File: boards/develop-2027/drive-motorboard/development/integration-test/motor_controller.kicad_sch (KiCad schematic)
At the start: 28 parts, among them U1 STSPIN32G0A2

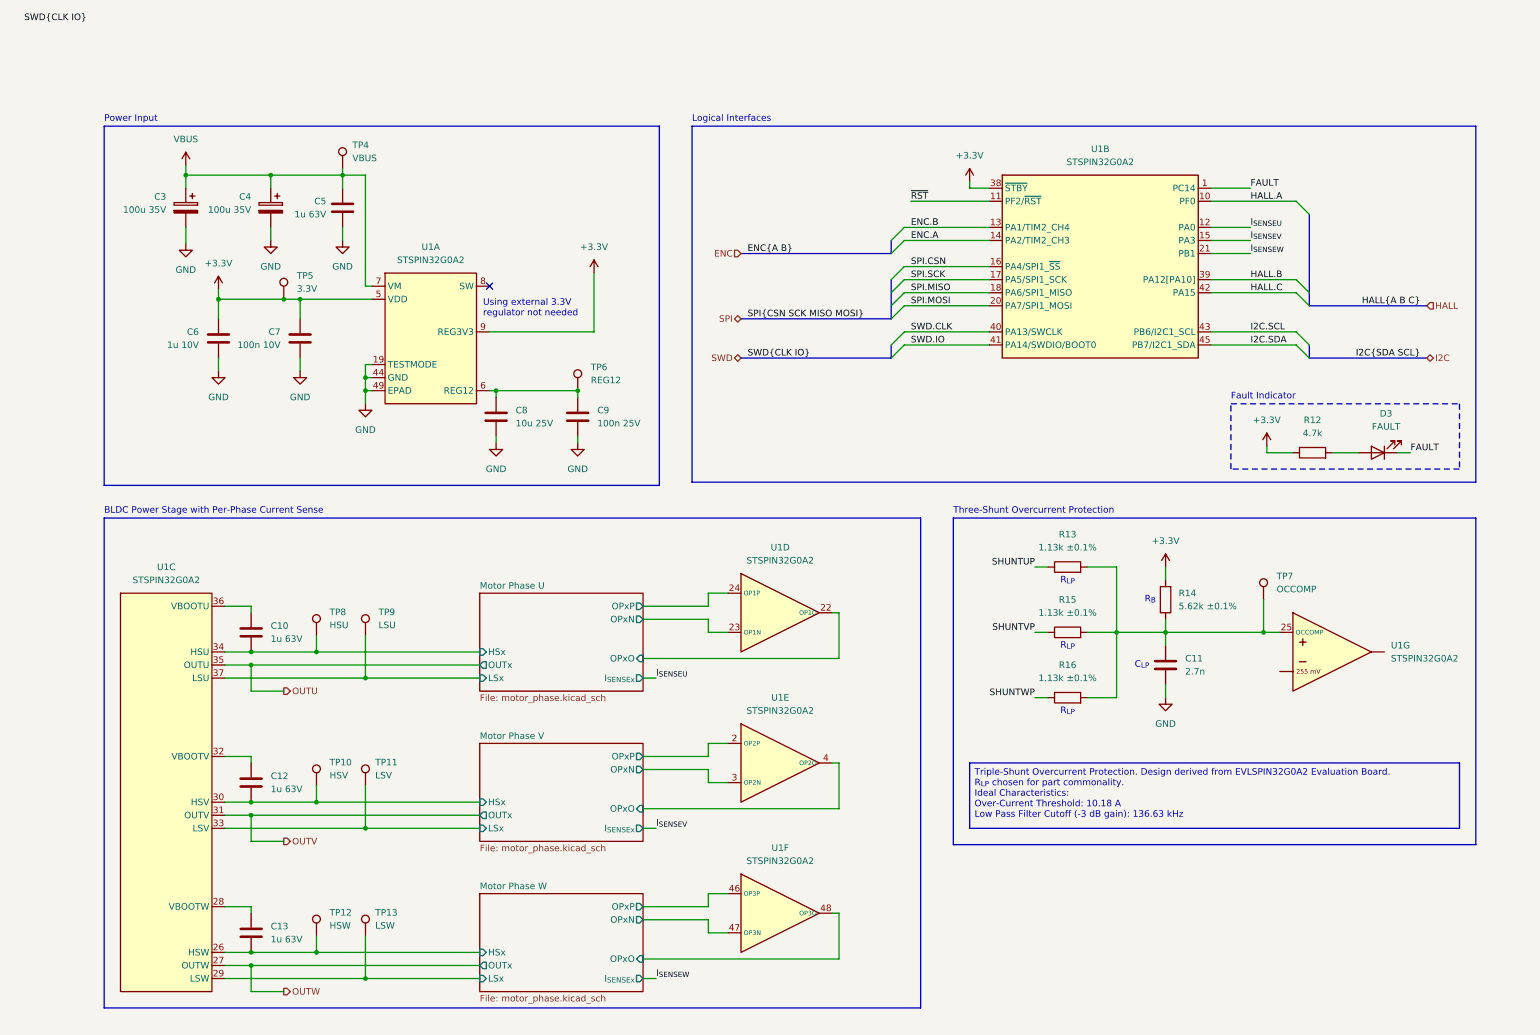
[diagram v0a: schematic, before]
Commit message: Resolve all ERC, tweak formatting
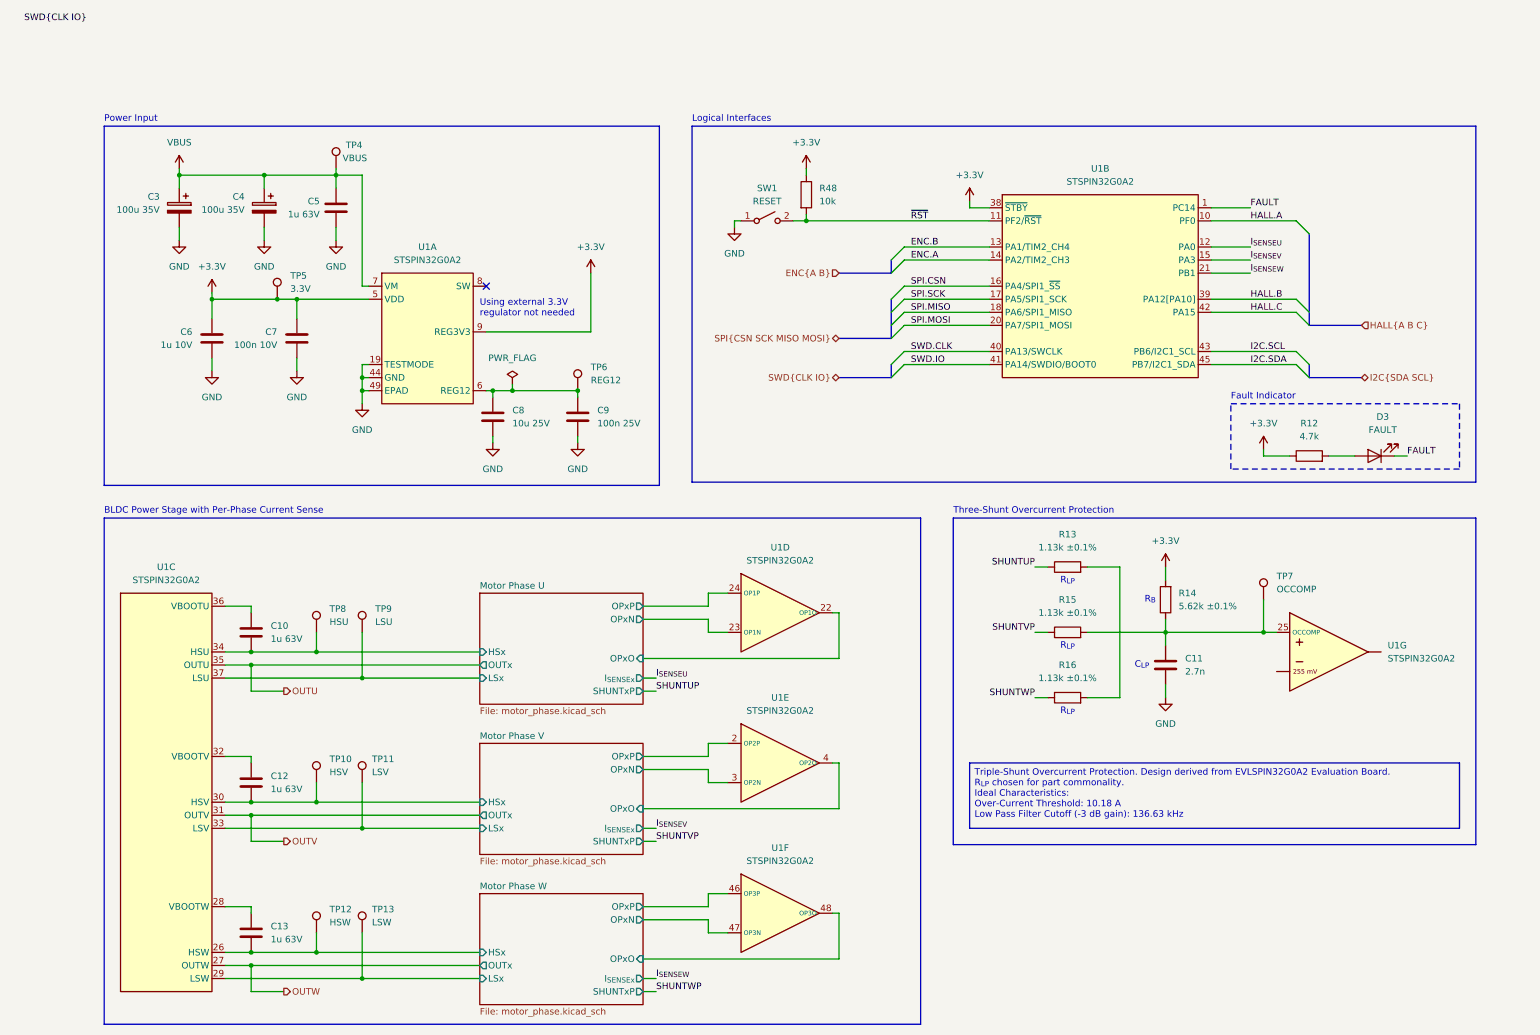
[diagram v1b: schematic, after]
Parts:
- added R48: 10k, Resistor_SMD:R_0402_1005Metric, symbol Device:R
- added SW1: RESET, Button_Switch_SMD:SW_Push_1P1T_NO_CK_KMR2, symbol Switch:SW_SPST
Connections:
- net +3.3V: now also R48.1
- net GND: now also SW1.1 (A)
- net ~{RST}: now also R48.2, SW1.2 (B)
- net at C11.1, R14.1, R15.2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: no longer R13.2, R16.2
- new net: R13.2, R16.2
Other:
- sheet Motor Phase U ports: added SHUNTxP; removed none
- sheet Motor Phase V ports: added SHUNTxP; removed none
- sheet Motor Phase W ports: added SHUNTxP; removed none
- moved on the sheet: C3, C4, C5, C6, C7, C8, D3, R12, TP10, TP11, TP12, TP13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

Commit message: tweak issues found during review, prep for single-shunt current sense
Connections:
- net ENC.A: now also U1.18 (PA6/TIM3_CH1); no longer U1.14 (PA2/TIM2_CH3)
- net ENC.B: now also U1.20 (PA7/TIM3_CH2); no longer U1.13 (PA1/TIM2_CH4)
- net HALL.A: now also U1.12 (PA0/TIM2_CH1); no longer U1.10 (PF0)
- net HALL.B: now also U1.13 (PA1/TIM2_CH2); no longer U1.39 (PA12[PA10])
- net HALL.C: now also U1.14 (PA2/TIM2_CH3); no longer U1.42 (PA15)
- net I_{SENSEU}: no longer U1.12 (PA0)
- net I_{SENSEV}: no longer U1.15 (PA3)
- net I_{SENSEW}: no longer U1.21 (PB1)
- net SPI.MISO: now also U1.15 (PA3/SPI2_MISO); no longer U1.18 (PA6/SPI1_MISO)
- net SPI.MOSI: now also U1.39 (PA12[PA10]/SPI2_MOSI); no longer U1.20 (PA7/SPI1_MOSI)
- new net I_{SENSE}: U1.21 (PB1)
- no-connect marks 1 -> 3
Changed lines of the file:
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@@
 		(at 90.17 53.34)
+	)
+	(no_connect
+		(at 231.14 40.64)
+	)
+	(no_connect
+		(at 231.14 55.88)
 	)
 	(bus_entry
@@
 	)
 	(bus_entry
-		(at 247.65 55.88)
+		(at 247.65 48.26)
 		(size 2.54 2.54)
 		(stroke
@@
 	)
 	(bus_entry
-		(at 247.65 58.42)
+		(at 247.65 50.8)
 		(size 2.54 2.54)
 		(stroke
@@
 	)
 	(bus_entry
-		(at 247.65 40.64)
+		(at 247.65 45.72)
 		(size 2.54 2.54)
 		(stroke
@@
 	(wire
 		(pts
-			(xy 231.14 55.88) (xy 247.65 55.88)
+			(xy 231.14 48.26) (xy 247.65 48.26)
 		)
 		(stroke
@@
 	(wire
 		(pts
+			(xy 231.14 60.96) (xy 238.76 60.96)
+		)
+		(stroke
+			(width 0)
+			(type default)
+		)
+	)
+	(wire
+		(pts
 			(xy 241.3 85.09) (xy 241.3 86.36)
 		)
@@
 	(wire
 		(pts
-			(xy 231.14 58.42) (xy 247.65 58.42)
+			(xy 231.14 50.8) (xy 247.65 50.8)
 		)
 		(stroke
@@
 	(wire
 		(pts
-			(xy 231.14 50.8) (xy 238.76 50.8)
-		)
-		(stroke
-			(width 0)
-			(type default)
-		)
-	)
-	(wire
-		(pts
 			(xy 50.8 161.29) (xy 44.45 161.29)
 		)
@@
 	(wire
 		(pts
-			(xy 231.14 48.26) (xy 238.76 48.26)
-		)
-		(stroke
-			(width 0)
-			(type default)
-		)
-	)
-	(wire
-		(pts
 			(xy 231.14 68.58) (xy 247.65 68.58)
 		)
@@
 	(wire
 		(pts
-			(xy 231.14 45.72) (xy 238.76 45.72)
-		)
-		(stroke
-			(width 0)
-			(type default)
-		)
-	)
-	(wire
-		(pts
 			(xy 44.45 132.08) (xy 44.45 127)
 		)
@@
 		)
 	)
+	(wire
+		(pts
+			(xy 196.85 120.65) (xy 199.39 120.65)
+		)
+		(stroke
+			(width 0)
+			(type default)
+		)
+	)
+	(wire
+		(pts
+			(xy 30.48 30.48) (xy 30.48 31.75)
+		)
+		(stroke
+			(width 0)
+			(type default)
+		)
+	)
+	(wire
+		(pts
+			(xy 231.14 45.72) (xy 247.65 45.72)
+		)
+		(stroke
+			(width 0)
+			(type default)
+		)
+	)
+	(wire
+		(pts
+			(xy 36.83 55.88) (xy 36.83 59.69)
+		)
+		(stroke
+			(width 0)
+			(type default)
+		)
+	)
+	(wire
+		(pts
+			(xy 207.01 107.95) (xy 213.36 107.95)
+		)
+		(stroke
+			(width 0)
+			(type default)
+		)
+	)
+	(wire
+		(pts
+			(xy 57.15 120.65) (xy 57.15 124.46)
+		)
+		(stroke
+			(width 0)
+			(type default)
+		)
+	)
 	(bus
 		(pts
-			(xy 260.35 60.96) (xy 250.19 60.96)
-		)
-		(stroke
-			(width 0)
-			(type default)
-		)
-	)
-	(wire
-		(pts
-			(xy 196.85 120.65) (xy 199.39 120.65)
-		)
-		(stroke
-			(width 0)
-			(type default)
-		)
-	)
-	(wire
-		(pts
-			(xy 30.48 30.48) (xy 30.48 31.75)
-		)
-		(stroke
-			(width 0)
-			(type default)
-		)
-	)
-	(wire
-		(pts
-			(xy 231.14 40.64) (xy 247.65 40.64)
-		)
-		(stroke
-			(width 0)
-			(type default)
-		)
-	)
-	(wire
-		(pts
-			(xy 36.83 55.88) (xy 36.83 59.69)
-		)
-		(stroke
-			(width 0)
-			(type default)
-		)
-	)
-	(wire
-		(pts
-			(xy 207.01 107.95) (xy 213.36 107.95)
-		)
-		(stroke
-			(width 0)
-			(type default)
-		)
-	)
-	(wire
-		(pts
-			(xy 57.15 120.65) (xy 57.15 124.46)
+			(xy 250.19 53.34) (xy 260.35 53.34)
 		)
 		(stroke
@@
 	(bus
 		(pts
-			(xy 250.19 43.18) (xy 250.19 60.96)
+			(xy 250.19 48.26) (xy 250.19 53.34)
 		)
 		(stroke
@@
 	)
 	(label "HALL.A"
-		(at 238.76 40.64 0)
-		(effects
-			(font
-				(size 1.27 1.27)
-			)
-			(justify left bottom)
-		)
-	)
-	(label "I_{SENSEW}"
-		(at 238.76 50.8 0)
+		(at 238.76 45.72 0)
 		(effects
 			(font
@@
 	)
 	(label "HALL.C"
-		(at 238.76 58.42 0)
+		(at 238.76 50.8 0)
 		(effects
 			(font
@@
 		)
 	)
-	(label "ENC.A"
-		(at 172.72 48.26 0)
-		(effects
-			(font
-				(size 1.27 1.27)
-			)
-			(justify left bottom)
-		)
-	)
 	(label "~{RST}"
 		(at 172.72 40.64 0)
@@
 		)
 	)
-	(label "ENC.B"
+	(label "ENC.A"
 		(at 172.72 45.72 0)
 		(effects
@@
 		)
 	)
-	(label "I_{SENSEV}"
-		(at 238.76 48.26 0)
-		(effects
-			(font
-				(size 1.27 1.27)
-			)
-			(justify left bottom)
-		)
-	)
 	(label "FAULT"
 		(at 238.76 38.1 0)
@@
 		)
 	)
-	(label "I_{SENSEU}"
-		(at 238.76 45.72 0)
+	(label "I_{SENSE}"
+		(at 238.76 60.96 0)
 		(effects
 			(font
@@
 		)
 	)
+	(label "ENC.B"
+		(at 172.72 48.26 0)
+		(effects
+			(font
+				(size 1.27 1.27)
+			)
+			(justify left bottom)
+		)
+	)
 	(label "HALL.B"
-		(at 238.76 55.88 0)
+		(at 238.76 48.26 0)
 		(effects
 			(font
@@
 	(hierarchical_label "HALL{A B C}"
 		(shape input)
-		(at 260.35 60.96 0)
+		(at 260.35 53.34 0)
 		(effects
 			(font
@@
 	)
 	(symbol
+		(lib_name "STSPIN32G0A2_1")
 		(lib_id "RJ-MCU:STSPIN32G0A2")
 		(at 209.55 48.26 0)
